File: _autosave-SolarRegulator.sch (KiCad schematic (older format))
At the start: 0 parts

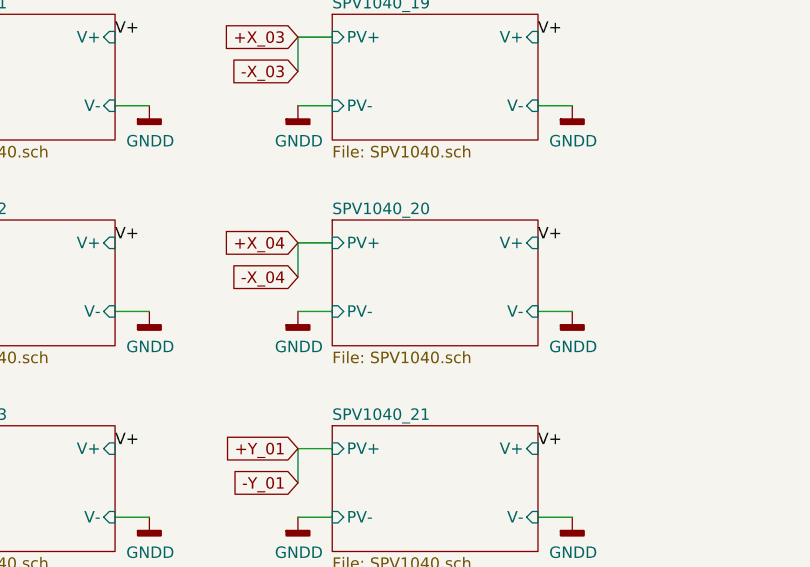
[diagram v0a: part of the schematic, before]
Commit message: Revisions to battery charge and discharge control. SPV1040 now regulates to 4.2V.
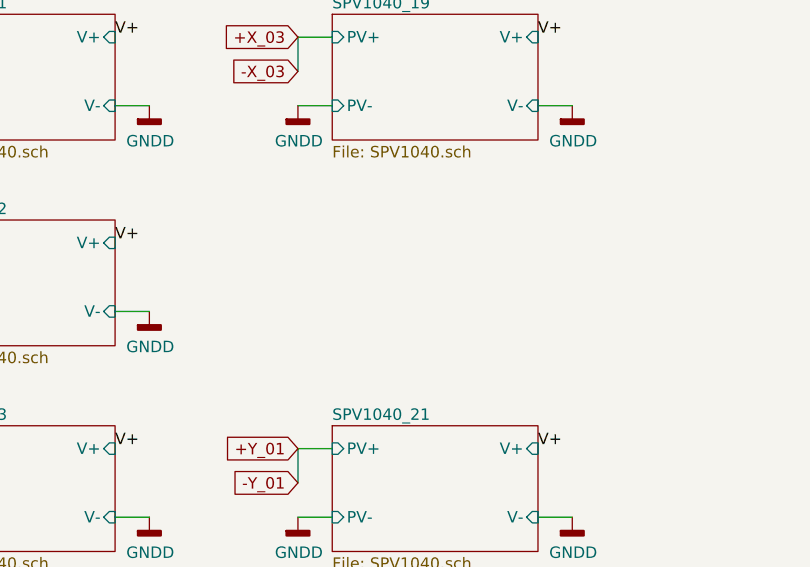
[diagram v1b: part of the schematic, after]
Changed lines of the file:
@@
 $Descr A4 11693 8268
 encoding utf-8
-Sheet 2 34
+Sheet 2 57
 Title "Electrical Power System"
 Date "2019-04-25"
@@
 Text GLabel 4400 2800 0    50   Input ~ 0
 -X_03
-$Sheet
-S 4550 3450 900  550
-U 5CCB70B2
-F0 "SPV1040_20" 50
-F1 "SPV1040.sch" 50
-F2 "PV+" I L 4550 3550 50
-F3 "PV-" I L 4550 3850 50
-F4 "V+" I R 5450 3550 50
-F5 "V-" I R 5450 3850 50
-$EndSheet
-Wire Wire Line
-	5450 3850 5600 3850
-$Comp
-L Main-rescue:GNDD-power #PWR?
-U 1 1 5CCB70BA
-P 4400 3850
-F 0 "#PWR?" H 4400 3600 50  0001 C CNN
-F 1 "GNDD" H 4404 3695 50  0000 C CNN
-F 2 "" H 4400 3850 50  0001 C CNN
-F 3 "" H 4400 3850 50  0001 C CNN
-	1    4400 3850
-	1    0    0    -1
-$EndComp
-Wire Wire Line
-	4400 3850 4550 3850
-Wire Wire Line
-	4550 3550 4400 3550
-Wire Wire Line
-	4400 3550 4400 3700
-Text GLabel 4400 3550 0    50   Input ~ 0
-+X_04
-Text GLabel 4400 3700 0    50   Input ~ 0
--X_04
-$Comp
-L Main-rescue:GNDD-power #PWR?
-U 1 1 5CCB70C5
-P 5600 3850
-F 0 "#PWR?" H 5600 3600 50  0001 C CNN
-F 1 "GNDD" H 5604 3695 50  0000 C CNN
-F 2 "" H 5600 3850 50  0001 C CNN
-F 3 "" H 5600 3850 50  0001 C CNN
-	1    5600 3850
-	1    0    0    -1
-$EndComp
 $Sheet
 S 4550 4350 900  550
@@
 Text Label 5450 2650 0    50   ~ 0
 V+
-Text Label 5450 3550 0    50   ~ 0
-V+
 Text Label 3600 3550 0    50   ~ 0
